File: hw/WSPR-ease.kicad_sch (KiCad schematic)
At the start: 44 parts, among them J101 pwr+data, J102 SMA, J103 SMA, Q101 MMBF170, U101 SRV05-4, U102 ESP32-S3-WROOM-1-N8R8, U103 LMR51430YDDCR, U104 GNSS module

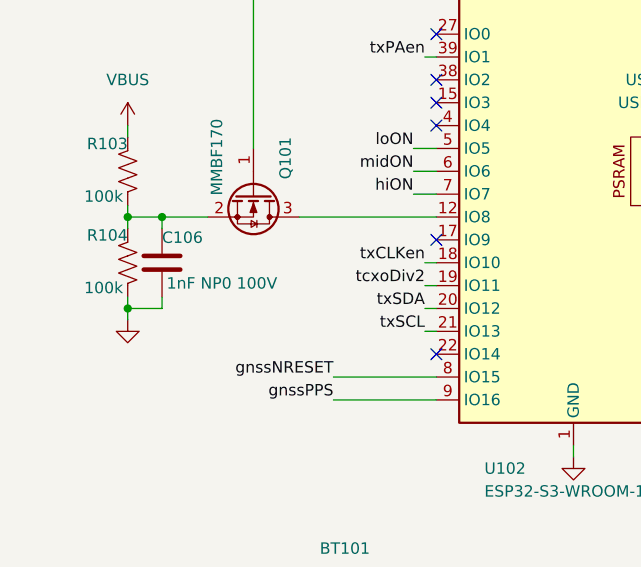
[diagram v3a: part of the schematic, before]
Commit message: Switch to SI5351C-B-GM for exciter + AHC to attenuate 3rd harmonic on a separate winding on the binocular transformer. Do so layout tweaks. This is much simpler than the FPGA version.
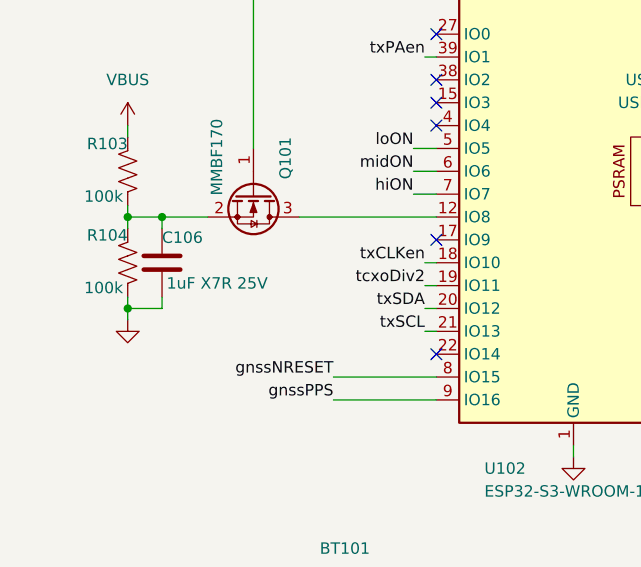
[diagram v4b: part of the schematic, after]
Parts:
- C106: value 1nF NP0 100V -> 1uF X7R 25V; footprint Capacitor_SMD:C_0603_1608Metric -> Capacitor_SMD:C_0402_1005Metric; MPN KGM15ACG2A102FT -> 04023D105MAT2A; Mouser_PN 581-KGM15ACG2A102FT -> 581-04023D105MAT2A
- C112: footprint Capacitor_SMD:C_0603_1608Metric -> Capacitor_SMD:C_0402_1005Metric; MPN CM105X7R105K25AT -> 04023D105MAT2A; Mouser_PN 346-CM105X7R105K25AT -> 581-04023D105MAT2A; cap-type (none) -> X5R
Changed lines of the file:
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@@
 			)
 		)
-		(property "Value" "1nF NP0 100V"
+		(property "Value" "1uF X7R 25V"
 			(at 28.448 86.106 0)
 			(effects
@@
 			)
 		)
-		(property "Footprint" "Capacitor_SMD:C_0603_1608Metric"
+		(property "Footprint" "Capacitor_SMD:C_0402_1005Metric"
 			(at 28.9052 87.63 0)
 			(effects
@@
 			)
 		)
-		(property "MPN" "KGM15ACG2A102FT"
+		(property "MPN" "04023D105MAT2A"
 			(at 27.94 83.82 0)
 			(effects
@@
 			)
 		)
-		(property "Mouser_PN" "581-KGM15ACG2A102FT"
+		(property "Mouser_PN" "581-04023D105MAT2A "
 			(at 27.94 83.82 0)
 			(effects
@@
 			)
 		)
-		(property "Footprint" "Capacitor_SMD:C_0603_1608Metric"
+		(property "Footprint" "Capacitor_SMD:C_0402_1005Metric"
 			(at 178.1048 156.21 0)
 			(effects
@@
 			)
 		)
-		(property "MPN" "CM105X7R105K25AT"
+		(property "MPN" "04023D105MAT2A"
 			(at 124.46 115.57 0)
 			(effects
@@
 			)
 		)
-		(property "Mouser_PN" "346-CM105X7R105K25AT"
+		(property "Mouser_PN" "581-04023D105MAT2A "
 			(at 124.46 115.57 0)
 			(effects
@@
 			)
 		)
-		(property "cap-type" ""
+		(property "cap-type" "X5R"
 			(at 181.864 156.464 0)
 			(effects

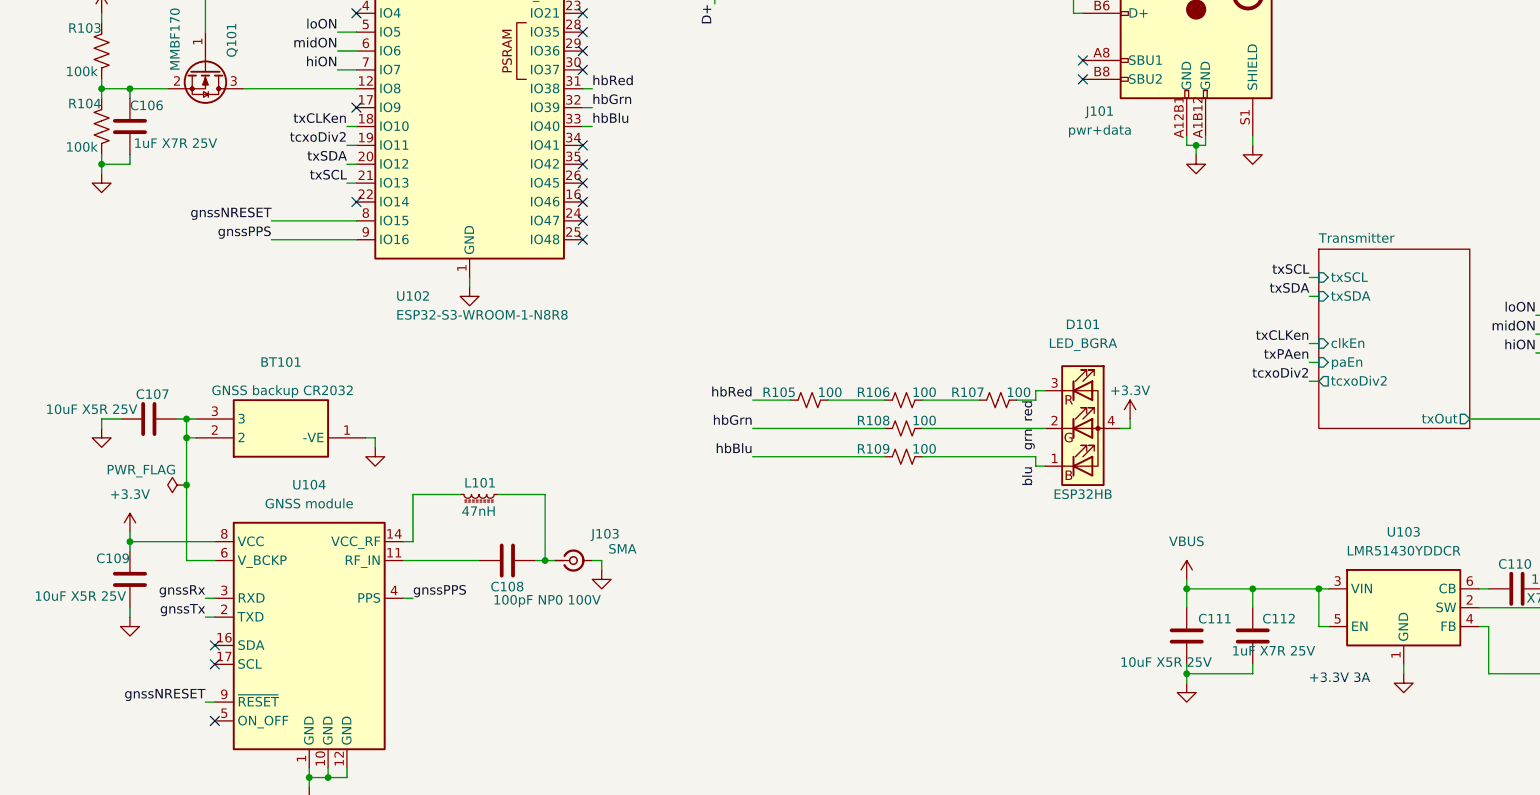
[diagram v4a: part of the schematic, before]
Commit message: Horsing around with JLCPCB assembly and BOM. I think it is still too expensive to do it this way for p1 build
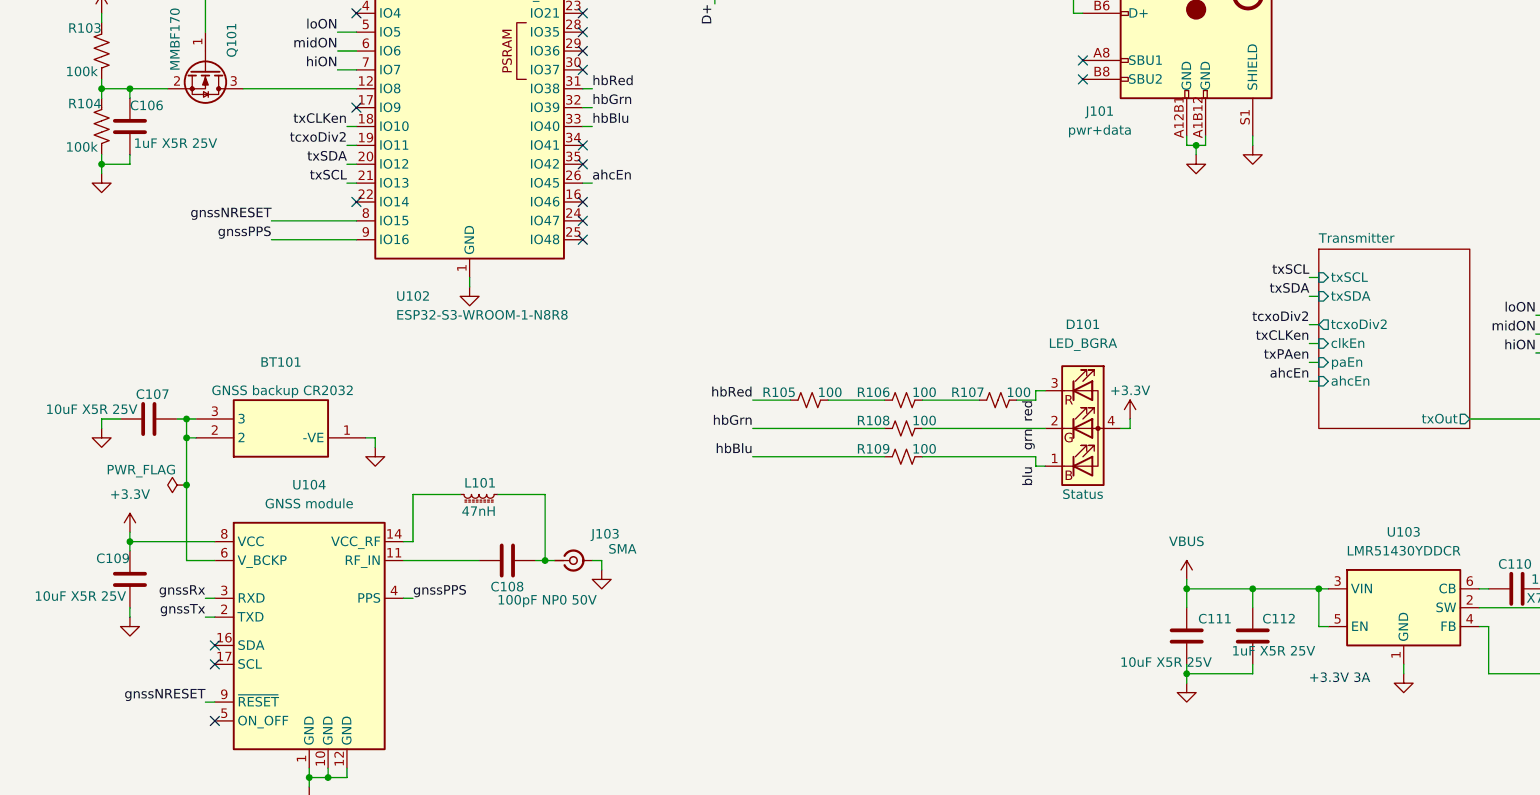
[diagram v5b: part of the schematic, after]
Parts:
- BT101: LCSC C6750449 -> C5904513
- C101, C103: LCSC C24452 -> C14663
- C102, C105, C107, C109, C113, C114: LCSC C96446 -> C479655; cap-type (none) -> X5R
- C104: footprint Capacitor_SMD:C_Elec_8x6.2 -> Capacitor_SMD:C_Elec_6.3x7.7; LCSC C1849748 -> C46528074; MFG Vishay -> Chemi-Con; MPN MAL214297007E3 -> HHXJ350ARA101MF80G; Mouser_PN 71-MAL214297007E3 -> 661-HHXJ350A101MF80G; working-voltage (none) -> 35V
- C106: value 1uF X7R 25V -> 1uF X5R 25V; LCSC C5182455 -> C7393852
- C108: value 100pF NP0 100V -> 100pF NP0 50V; LCSC C106200 -> C76709; cap-type (none) -> NP0; working-voltage (none) -> 50V
- C110: LCSC C24452 -> C14663; LCSC_PN C24452 -> (none)
- C111: LCSC C96446 -> C479655; LCSC_PN C327087 -> (none); cap-type (none) -> X5R
- C112: value 1uF X7R 25V -> 1uF X5R 25V; LCSC C14445 -> C7393852; LCSC_PN C301928 -> (none)
- D101: LCSC (none) -> C5333730; label ESP32HB -> Status
- J101: LCSC (none) -> C45082769; MFG (none) -> Same Sky; MPN UJ20-C-H-G-SMT-2A-P16-TR -> UJ20-C-H-G-SMT-P16-TR; Mouser_PN 179-CHGSMT2AP16TR -> 179-UJ20CHGSMTP16TR
- L102: LCSC C48689537 -> C5349606; LCSC_PN C86089 -> (none); MFG Abracon -> APV; MPN AIML-1008HC-2R2M-T -> APH252010T2R2M; Manufacturer muRata -> APV; Mouser_PN 815-AIML-1008HC2R2MT -> (none); Part Number LQM21PN2R2NGCD -> APH252010T2R2M
- Q101: LCSC C28871 -> C151058
- R101, R102: LCSC C105872 -> C2906874; LCSC_PN C854378 -> (none)
- R103, R104: LCSC C60491 -> C2906859
- R105, R106, R107, R108, R109: LCSC (none) -> C2906860
- R110: LCSC C60491 -> C2906859; LCSC_PN C728576 -> (none)
- R111: LCSC C82868 -> C2929993; LCSC_PN C284424 -> (none)
- U102: LCSC C2913204 -> C2913201
- U103: LCSC C5185863 -> C5210749; LCSC_PN C5185863 -> (none)
- U104: LCSC C90770 -> C2970256
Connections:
- net ahcEn: now reaches U102.26 (IO45)
- no-connect marks 25 -> 24
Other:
- sheet Transmitter ports: added ahcEn; removed none

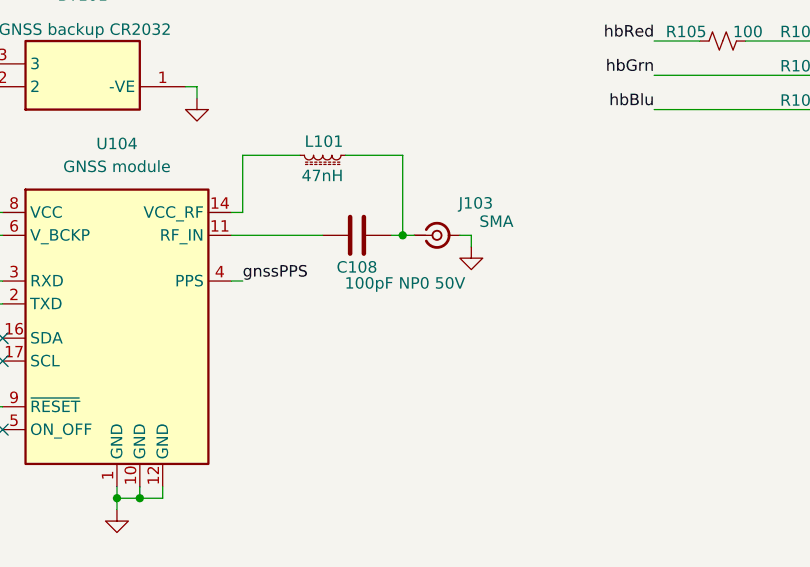
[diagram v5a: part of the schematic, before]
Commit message: OCD fixes. Fix USB2 connector footprint AGAIN (these things are not standardized!).
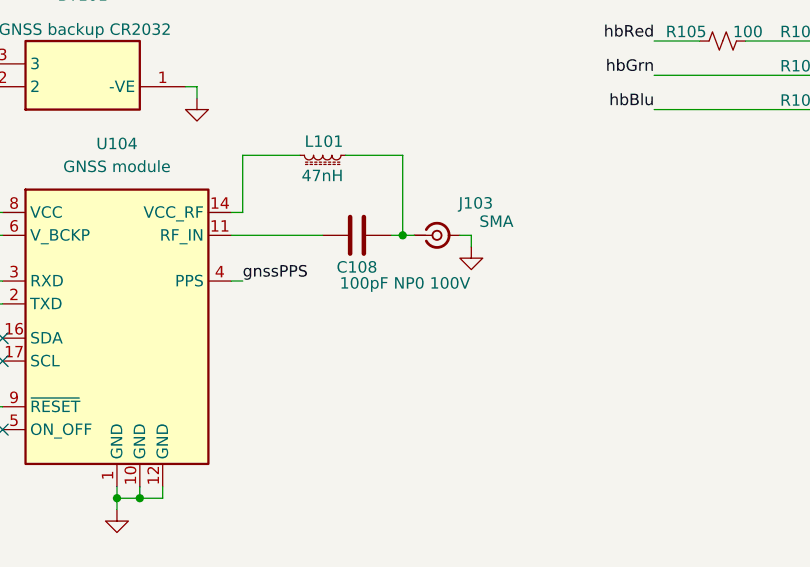
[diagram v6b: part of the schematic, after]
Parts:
- C108: value 100pF NP0 50V -> 100pF NP0 100V
- J101: footprint Library:USB_C_Receptacle_HRO_TYPE-C-31-M-12-bursted -> Library:UJ20-C-H-G-SMT-P16-TR
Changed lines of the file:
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@@
 			)
 		)
-		(property "Value" "100pF NP0 50V"
+		(property "Value" "100pF NP0 100V"
 			(at 84.074 147.574 90)
 			(effects
@@
 			)
 		)
-		(property "Footprint" "Library:USB_C_Receptacle_HRO_TYPE-C-31-M-12-bursted"
+		(property "Footprint" "Library:UJ20-C-H-G-SMT-P16-TR"
 			(at 167.64 62.23 0)
 			(effects
